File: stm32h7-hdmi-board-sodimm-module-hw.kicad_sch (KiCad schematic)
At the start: 8 parts

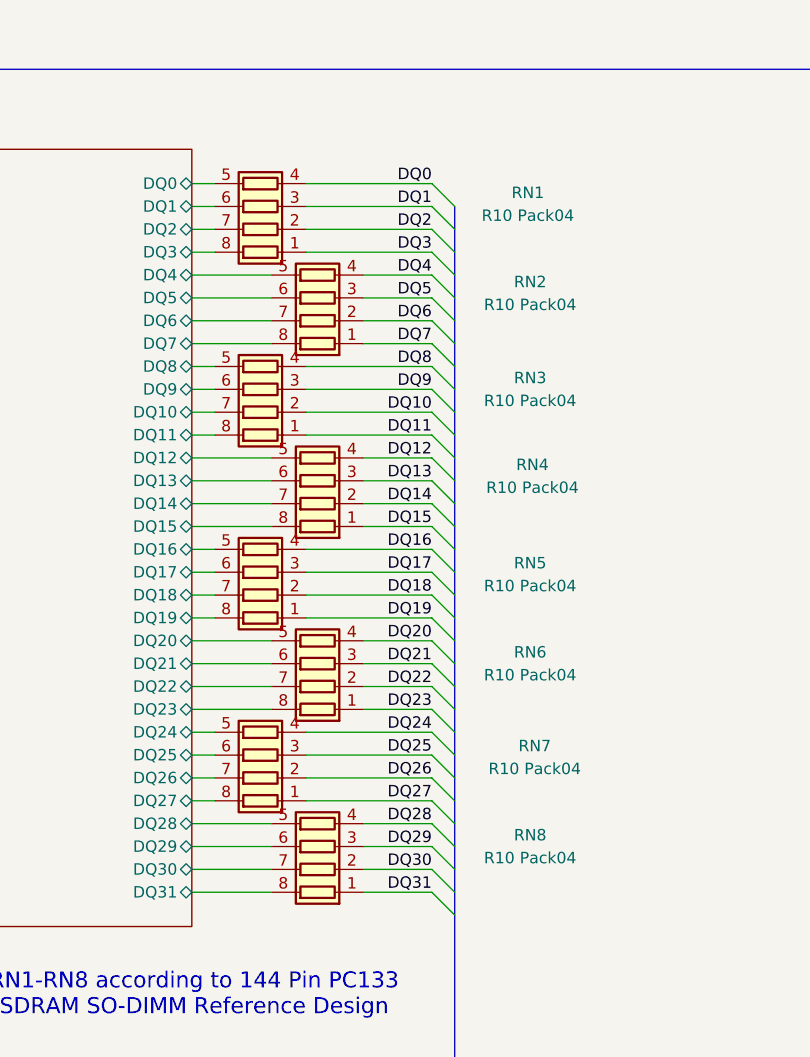
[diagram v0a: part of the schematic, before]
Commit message: [#100650] PCB layout update - placing ICs
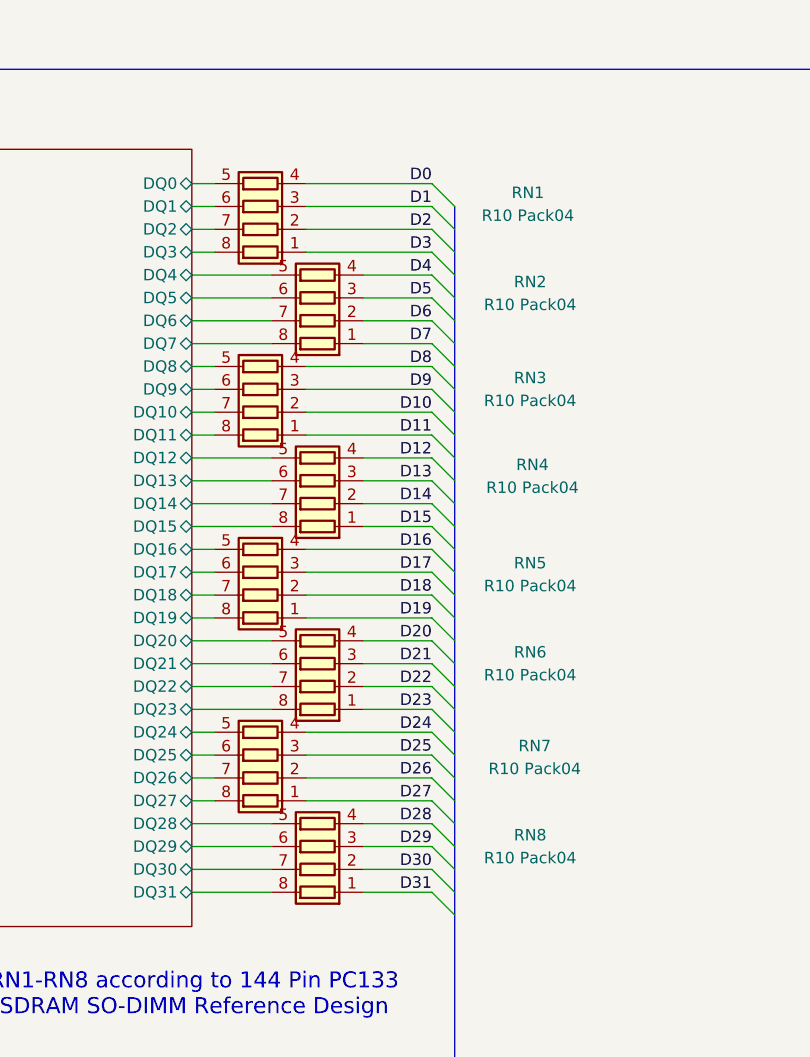
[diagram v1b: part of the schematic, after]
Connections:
- net DQ0 renamed D0
- net DQ1 renamed D1
- net DQ10 renamed D10
- net DQ11 renamed D11
- net DQ12 renamed D12
- net DQ13 renamed D13
- net DQ14 renamed D14
- net DQ15 renamed D15
- net DQ16 renamed D16
- net DQ17 renamed D17
- net DQ18 renamed D18
- net DQ19 renamed D19
- net DQ2 renamed D2
- net DQ20 renamed D20
- net DQ21 renamed D21
- net DQ22 renamed D22
- net DQ23 renamed D23
- net DQ24 renamed D24
- net DQ25 renamed D25
- net DQ26 renamed D26
- net DQ27 renamed D27
- net DQ28 renamed D28
- net DQ29 renamed D29
- net DQ3 renamed D3
- net DQ30 renamed D30
- net DQ31 renamed D31
- net DQ4 renamed D4
- net DQ5 renamed D5
- net DQ6 renamed D6
- net DQ7 renamed D7
- net DQ8 renamed D8
- net DQ9 renamed D9
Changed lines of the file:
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@@
 		)
 	)
-	(label "DQ29"
+	(label "D29"
 		(at 139.7 167.64 180)
 		(effects
@@
 		)
 	)
-	(label "DQ18"
+	(label "D18"
 		(at 139.7 139.7 180)
 		(effects
@@
 		)
 	)
-	(label "DQ7"
+	(label "D7"
 		(at 139.7 111.76 180)
 		(effects
@@
 		)
 	)
-	(label "DQ22"
+	(label "D22"
 		(at 139.7 149.86 180)
 		(effects
@@
 		)
 	)
-	(label "DQ14"
+	(label "D14"
 		(at 139.7 129.54 180)
 		(effects
@@
 		)
 	)
-	(label "DQ21"
+	(label "D21"
 		(at 139.7 147.32 180)
 		(effects
@@
 		)
 	)
-	(label "DQ4"
+	(label "D4"
 		(at 139.7 104.14 180)
 		(effects
@@
 		)
 	)
-	(label "DQ6"
+	(label "D6"
 		(at 139.7 109.22 180)
 		(effects
@@
 		)
 	)
-	(label "DQ16"
+	(label "D16"
 		(at 139.7 134.62 180)
 		(effects
@@
 		)
 	)
-	(label "DQ2"
+	(label "D2"
 		(at 139.7 99.06 180)
 		(effects
@@
 		)
 	)
-	(label "DQ10"
+	(label "D10"
 		(at 139.7 119.38 180)
 		(effects
@@
 		)
 	)
-	(label "DQ9"
+	(label "D9"
 		(at 139.7 116.84 180)
 		(effects
@@
 		)
 	)
-	(label "DQ26"
+	(label "D26"
 		(at 139.7 160.02 180)
 		(effects
@@
 		)
 	)
-	(label "DQ13"
+	(label "D13"
 		(at 139.7 127 180)
 		(effects
@@
 		)
 	)
-	(label "DQ0"
+	(label "D0"
 		(at 139.7 93.98 180)
 		(effects
@@
 		)
 	)
-	(label "DQ8"
+	(label "D8"
 		(at 139.7 114.3 180)
 		(effects
@@
 		)
 	)
-	(label "DQ17"
+	(label "D17"
 		(at 139.7 137.16 180)
 		(effects
@@
 		)
 	)
-	(label "DQ12"
+	(label "D12"
 		(at 139.7 124.46 180)
 		(effects
@@
 		)
 	)
-	(label "DQ15"
+	(label "D15"
 		(at 139.7 132.08 180)
 		(effects
@@
 		)
 	)
-	(label "DQ25"
+	(label "D25"
 		(at 139.7 157.48 180)
 		(effects
@@
 		)
 	)
-	(label "DQ23"
+	(label "D23"
 		(at 139.7 152.4 180)
 		(effects
@@
 		)
 	)
-	(label "DQ3"
+	(label "D3"
 		(at 139.7 101.6 180)
 		(effects
@@
 		)
 	)
-	(label "DQ31"
+	(label "D31"
 		(at 139.7 172.72 180)
 		(effects
@@
 		)
 	)
-	(label "DQ27"
+	(label "D27"
 		(at 139.7 162.56 180)
 		(effects
@@
 		)
 	)
-	(label "DQ28"
+	(label "D28"
 		(at 139.7 165.1 180)
 		(effects
@@
 		)
 	)
-	(label "DQ24"
+	(label "D24"
 		(at 139.7 154.94 180)
 		(effects
@@
 		)
 	)
-	(label "DQ30"
+	(label "D30"
 		(at 139.7 170.18 180)
 		(effects
@@
 		)
 	)
-	(label "DQ11"
+	(label "D11"
 		(at 139.7 121.92 180)
 		(effects
@@
 		)
 	)
-	(label "DQ1"
+	(label "D1"
 		(at 139.7 96.52 180)
 		(effects
@@
 		)
 	)
-	(label "DQ20"
+	(label "D20"
 		(at 139.7 144.78 180)
 		(effects
@@
 		)
 	)
-	(label "DQ19"
+	(label "D19"
 		(at 139.7 142.24 180)
 		(effects
@@
 		)
 	)
-	(label "DQ5"
+	(label "D5"
 		(at 139.7 106.68 180)
 		(effects

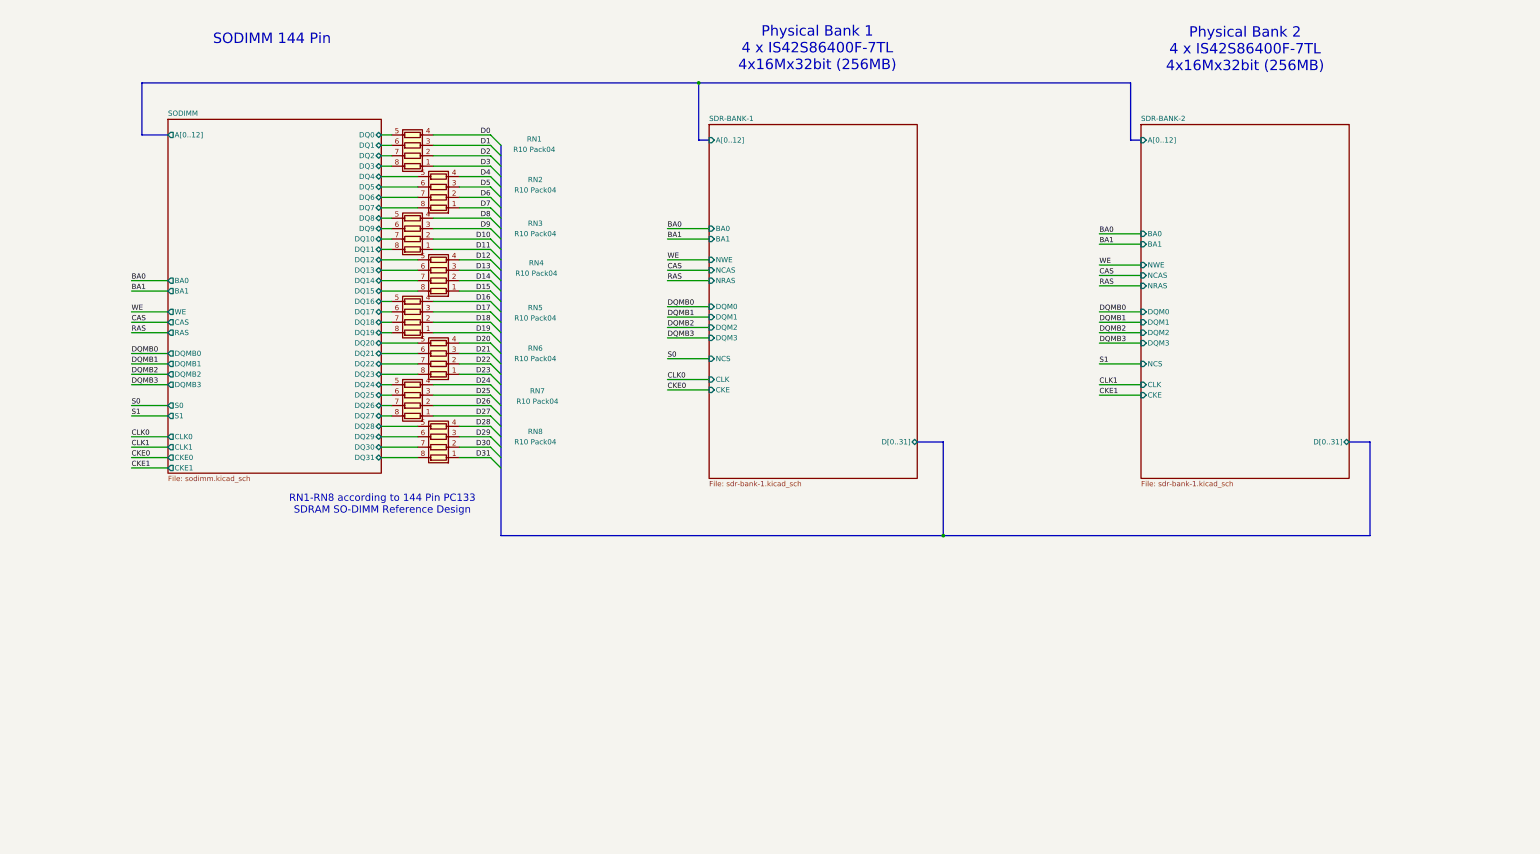
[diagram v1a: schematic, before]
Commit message: [#100470] Change schematic hierarchy
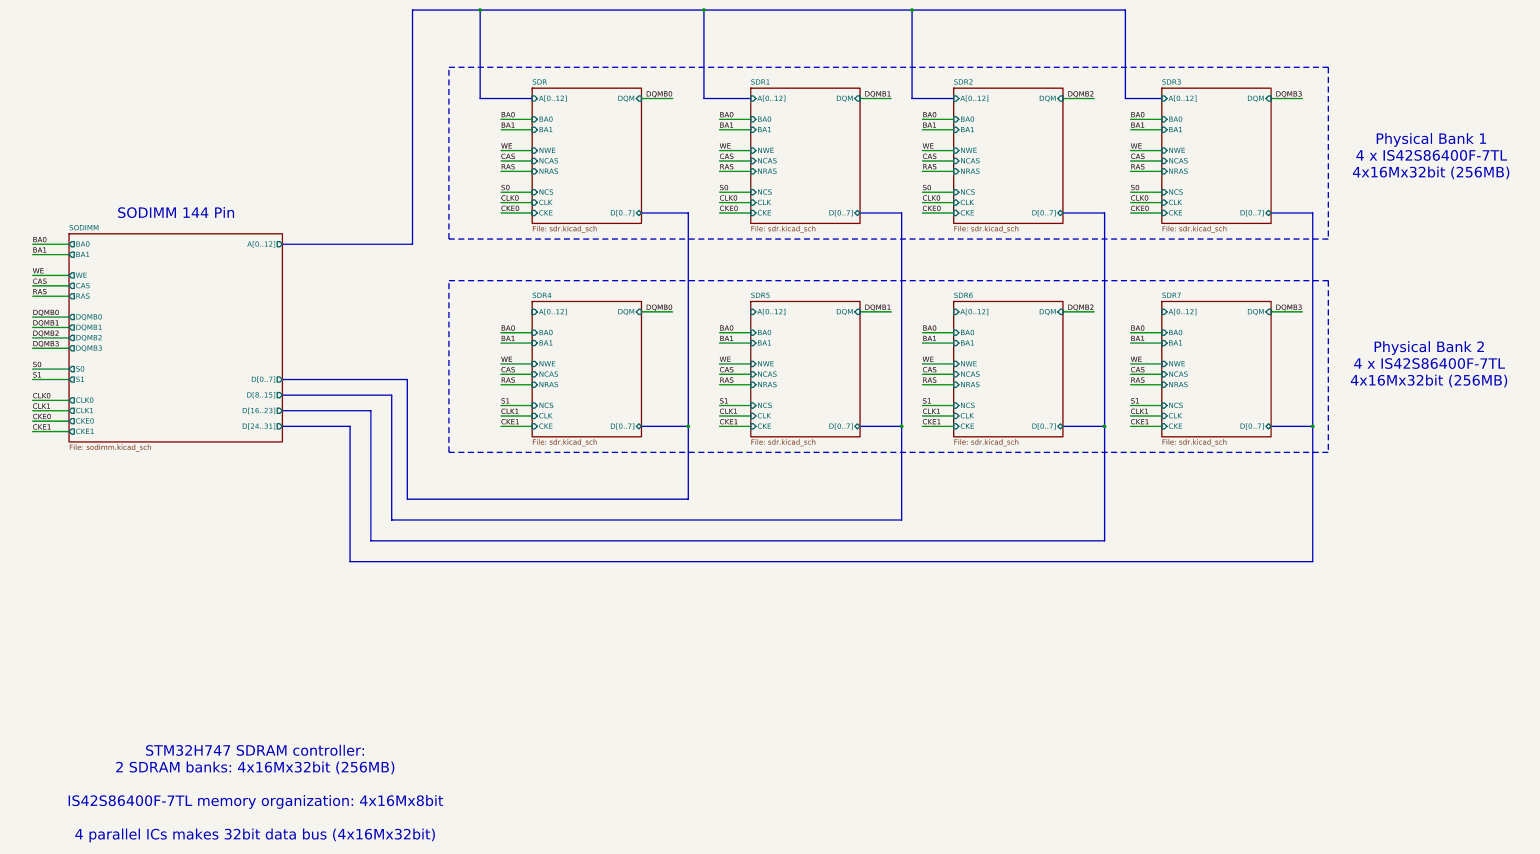
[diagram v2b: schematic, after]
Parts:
- removed RN1, RN2, RN3, RN4, RN5, RN6, RN7, RN8: R10 Pack04, Resistor_SMD:R_Array_Convex_4x0603, symbol Device:R_Pack04
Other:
- removed sheet SDR-BANK-1
- removed sheet SDR-BANK-2
- added sheet SDR (sdr.kicad_sch)
- added sheet SDR1 (sdr.kicad_sch)
- added sheet SDR2 (sdr.kicad_sch)
- added sheet SDR3 (sdr.kicad_sch)
- added sheet SDR4 (sdr.kicad_sch)
- added sheet SDR5 (sdr.kicad_sch)
- added sheet SDR6 (sdr.kicad_sch)
- added sheet SDR7 (sdr.kicad_sch)
- sheet SODIMM ports: added D[0..7], D[16..23], D[24..31], D[8..15]; removed DQ0, DQ1, DQ10, DQ11, DQ12, DQ13, DQ14, DQ15, DQ16, DQ17, DQ18, DQ19, DQ2, DQ20, DQ21, DQ22, DQ23, DQ24, DQ25, DQ26, DQ27, DQ28, DQ29, DQ3, DQ30, DQ31, DQ4, DQ5, DQ6, DQ7, DQ8, DQ9
- note added: "STM32H747 SDRAM controller: 2 SDRAM banks: 4x16Mx32bit (256MB) IS42S86400F-7TL memory organization: 4x16Mx8bit 4 parallel ICs makes 32bit data bus (4x16Mx32bit)"
- note removed: "RN1-RN8 according to 144 Pin PC133 SDRAM SO-DIMM Reference Design"

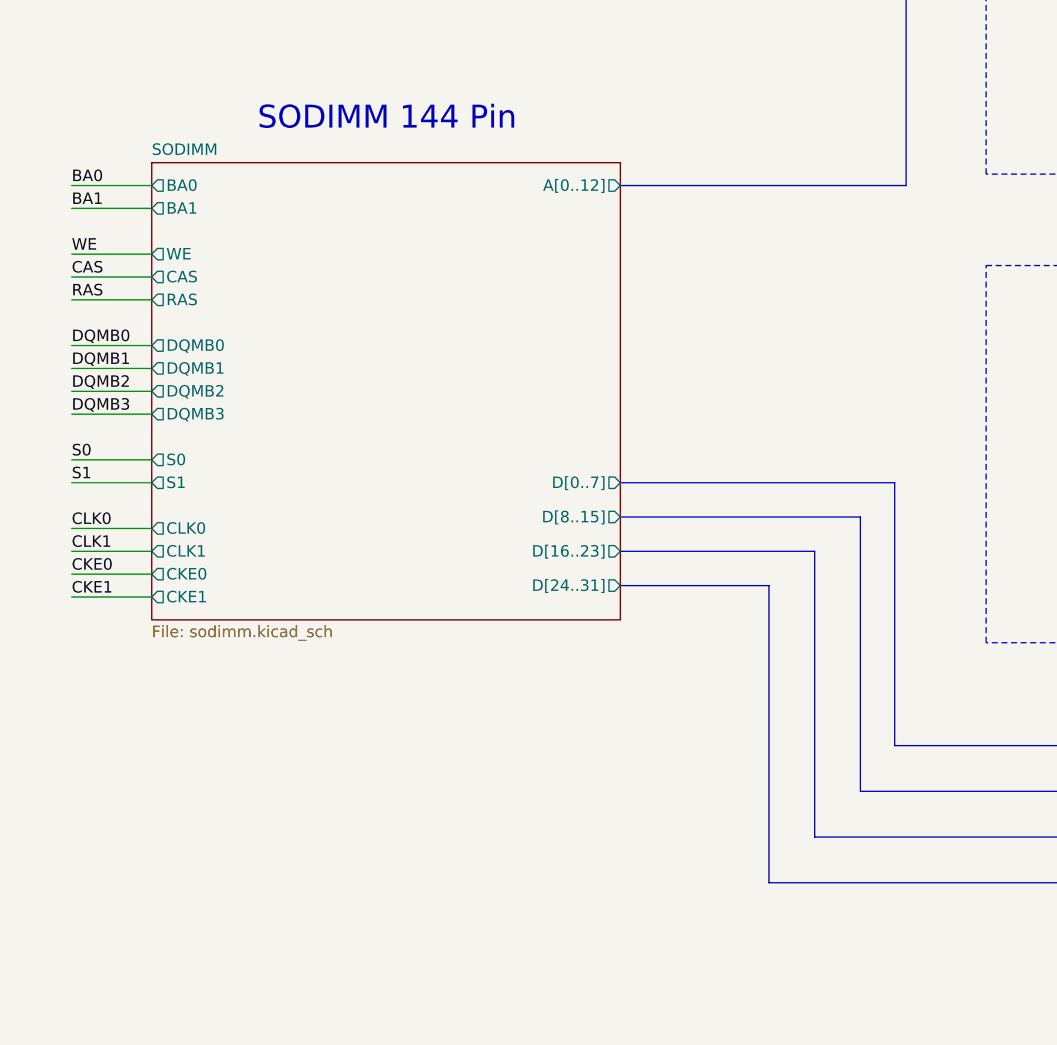
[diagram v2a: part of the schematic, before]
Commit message: [#100650] Add Antmicro logo
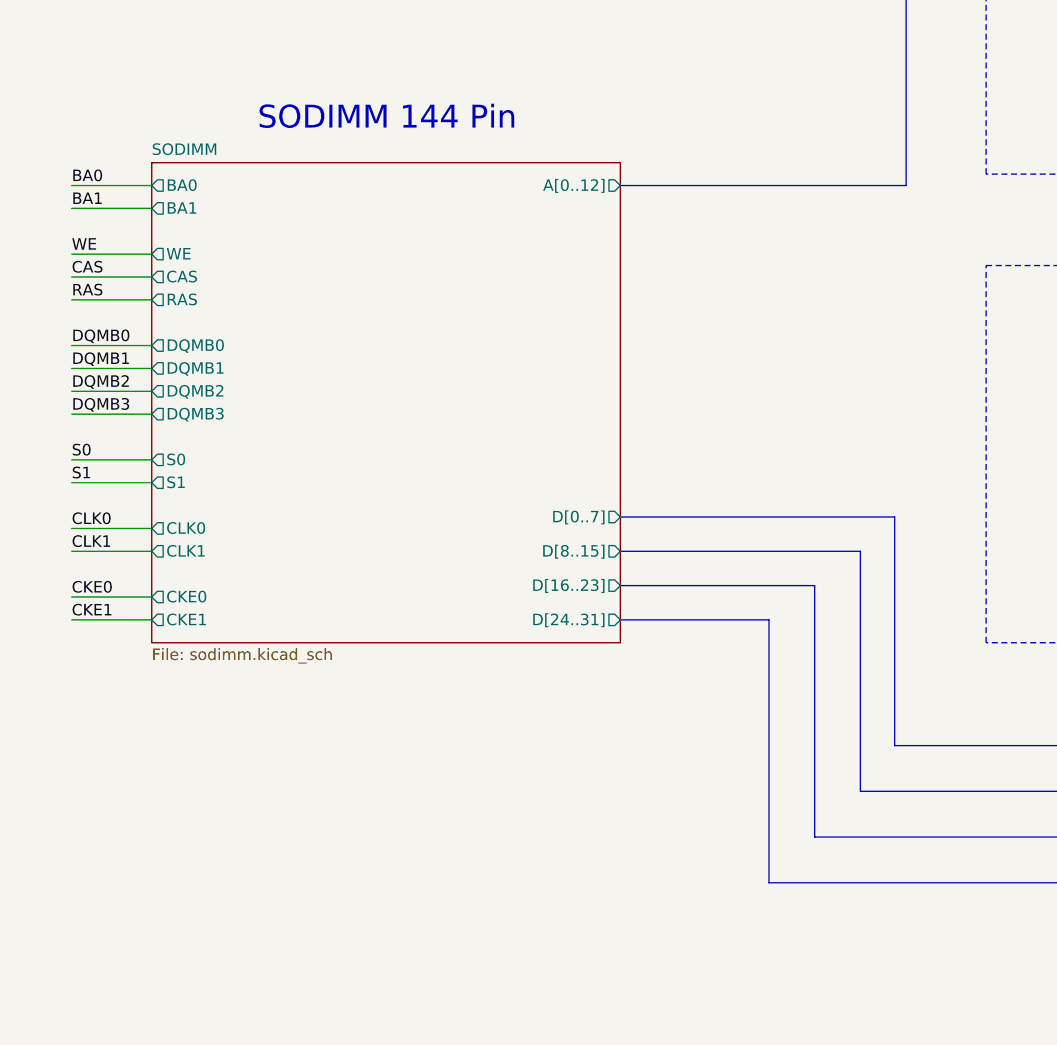
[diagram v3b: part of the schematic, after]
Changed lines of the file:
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@@
 	(bus
 		(pts
-			(xy 119.38 153.67) (xy 119.38 182.88)
+			(xy 119.38 157.48) (xy 119.38 182.88)
 		)
 		(stroke
@@
 	(bus
 		(pts
-			(xy 115.57 157.48) (xy 115.57 187.96)
+			(xy 115.57 161.29) (xy 115.57 187.96)
 		)
 		(stroke
@@
 	(bus
 		(pts
-			(xy 88.9 161.29) (xy 110.49 161.29)
+			(xy 88.9 165.1) (xy 110.49 165.1)
 		)
 		(stroke
@@
 	(bus
 		(pts
-			(xy 88.9 153.67) (xy 119.38 153.67)
+			(xy 88.9 157.48) (xy 119.38 157.48)
 		)
 		(stroke
@@
 	(bus
 		(pts
-			(xy 105.41 165.1) (xy 105.41 198.12)
+			(xy 105.41 168.91) (xy 105.41 198.12)
 		)
 		(stroke
@@
 	(wire
 		(pts
-			(xy 27.94 163.83) (xy 36.83 163.83)
+			(xy 27.94 166.37) (xy 36.83 166.37)
 		)
 		(stroke
@@
 	(bus
 		(pts
-			(xy 88.9 157.48) (xy 115.57 157.48)
+			(xy 88.9 161.29) (xy 115.57 161.29)
 		)
 		(stroke
@@
 	(bus
 		(pts
-			(xy 88.9 165.1) (xy 105.41 165.1)
+			(xy 88.9 168.91) (xy 105.41 168.91)
 		)
 		(stroke
@@
 	(bus
 		(pts
-			(xy 110.49 161.29) (xy 110.49 193.04)
+			(xy 110.49 165.1) (xy 110.49 193.04)
 		)
 		(stroke
@@
 	(wire
 		(pts
-			(xy 27.94 166.37) (xy 36.83 166.37)
+			(xy 27.94 168.91) (xy 36.83 168.91)
 		)
 		(stroke
@@
 	)
 	(label "CKE0"
-		(at 27.94 163.83 0)
+		(at 27.94 166.37 0)
 		(effects
 			(font
@@
 	)
 	(label "CKE1"
-		(at 27.94 166.37 0)
+		(at 27.94 168.91 0)
 		(effects
 			(font
@@
 			)
 			(justify left bottom)
+		)
+	)
+	(rule_area
+		(exclude_from_sim no)
+		(in_bom yes)
+		(on_board yes)
+		(dnp no)
+		(polyline
+			(pts
+				(xy 26.67 156.21) (xy 45.72 156.21) (xy 45.72 162.56) (xy 26.67 162.56)
+			)
+			(stroke
+				(width 0)
+				(type dash)
+			)
+			(fill
+				(type none)
+			)
+		)
+	)
+	(rule_area
+		(exclude_from_sim no)
+		(in_bom yes)
+		(on_board yes)
+		(dnp no)
+		(polyline
+			(pts
+				(xy 26.67 163.83) (xy 45.72 163.83) (xy 45.72 170.18) (xy 26.67 170.18)
+			)
+			(stroke
+				(width 0)
+				(type dash)
+			)
+			(fill
+				(type none)
+			)
+		)
+	)
+	(rule_area
+		(exclude_from_sim no)
+		(in_bom yes)
+		(on_board yes)
+		(dnp no)
+		(polyline
+			(pts
+				(xy 26.67 135.89) (xy 45.72 135.89) (xy 45.72 147.32) (xy 26.67 147.32)
+			)
+			(stroke
+				(width 0)
+				(type dash)
+			)
+			(fill
+				(type none)
+			)
+		)
+	)
+	(rule_area
+		(exclude_from_sim no)
+		(in_bom yes)
+		(on_board yes)
+		(dnp no)
+		(polyline
+			(pts
+				(xy 26.67 148.59) (xy 45.72 148.59) (xy 45.72 154.94) (xy 26.67 154.94)
+			)
+			(stroke
+				(width 0)
+				(type dash)
+			)
+			(fill
+				(type none)
+			)
+		)
+	)
+	(rule_area
+		(exclude_from_sim no)
+		(in_bom yes)
+		(on_board yes)
+		(dnp no)
+		(polyline
+			(pts
+				(xy 91.44 170.18) (xy 77.47 170.18) (xy 77.47 154.94) (xy 91.44 154.94)
+			)
+			(stroke
+				(width 0)
+				(type dash)
+			)
+			(fill
+				(type none)
+			)
 		)
 	)
@@
 	(sheet
 		(at 36.83 118.11)
-		(size 52.07 50.8)
+		(size 52.07 53.34)
 		(exclude_from_sim no)
 		(in_bom yes)
@@
 		)
 		(property "Sheetfile" "sodimm.kicad_sch"
-			(at 36.83 169.4946 0)
+			(at 36.83 172.0346 0)
 			(show_name no)
 			(do_not_autoplace no)
@@
 		)
 		(pin "CKE0" output
-			(at 36.83 163.83 180)
+			(at 36.83 166.37 180)
 			(effects
 				(font
@@
 		)
 		(pin "CKE1" output
-			(at 36.83 166.37 180)
+			(at 36.83 168.91 180)
 			(effects
 				(font
@@
 		)
 		(pin "D[0..7]" output
-			(at 88.9 153.67 0)
+			(at 88.9 157.48 0)
 			(effects
 				(font
@@
 		)
 		(pin "D[8..15]" output
-			(at 88.9 157.48 0)
+			(at 88.9 161.29 0)
 			(effects
 				(font
@@
 		)
 		(pin "D[16..23]" output
-			(at 88.9 161.29 0)
+			(at 88.9 165.1 0)
 			(effects
 				(font
@@
 		)
 		(pin "D[24..31]" output
-			(at 88.9 165.1 0)
-			(effects
-				(font
+			(at 88.9 168.91 0)
+			(effects
+				(font
